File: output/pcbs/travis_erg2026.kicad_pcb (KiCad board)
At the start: 2 copper layers, 163.7 x 159.6 mm, 161 parts

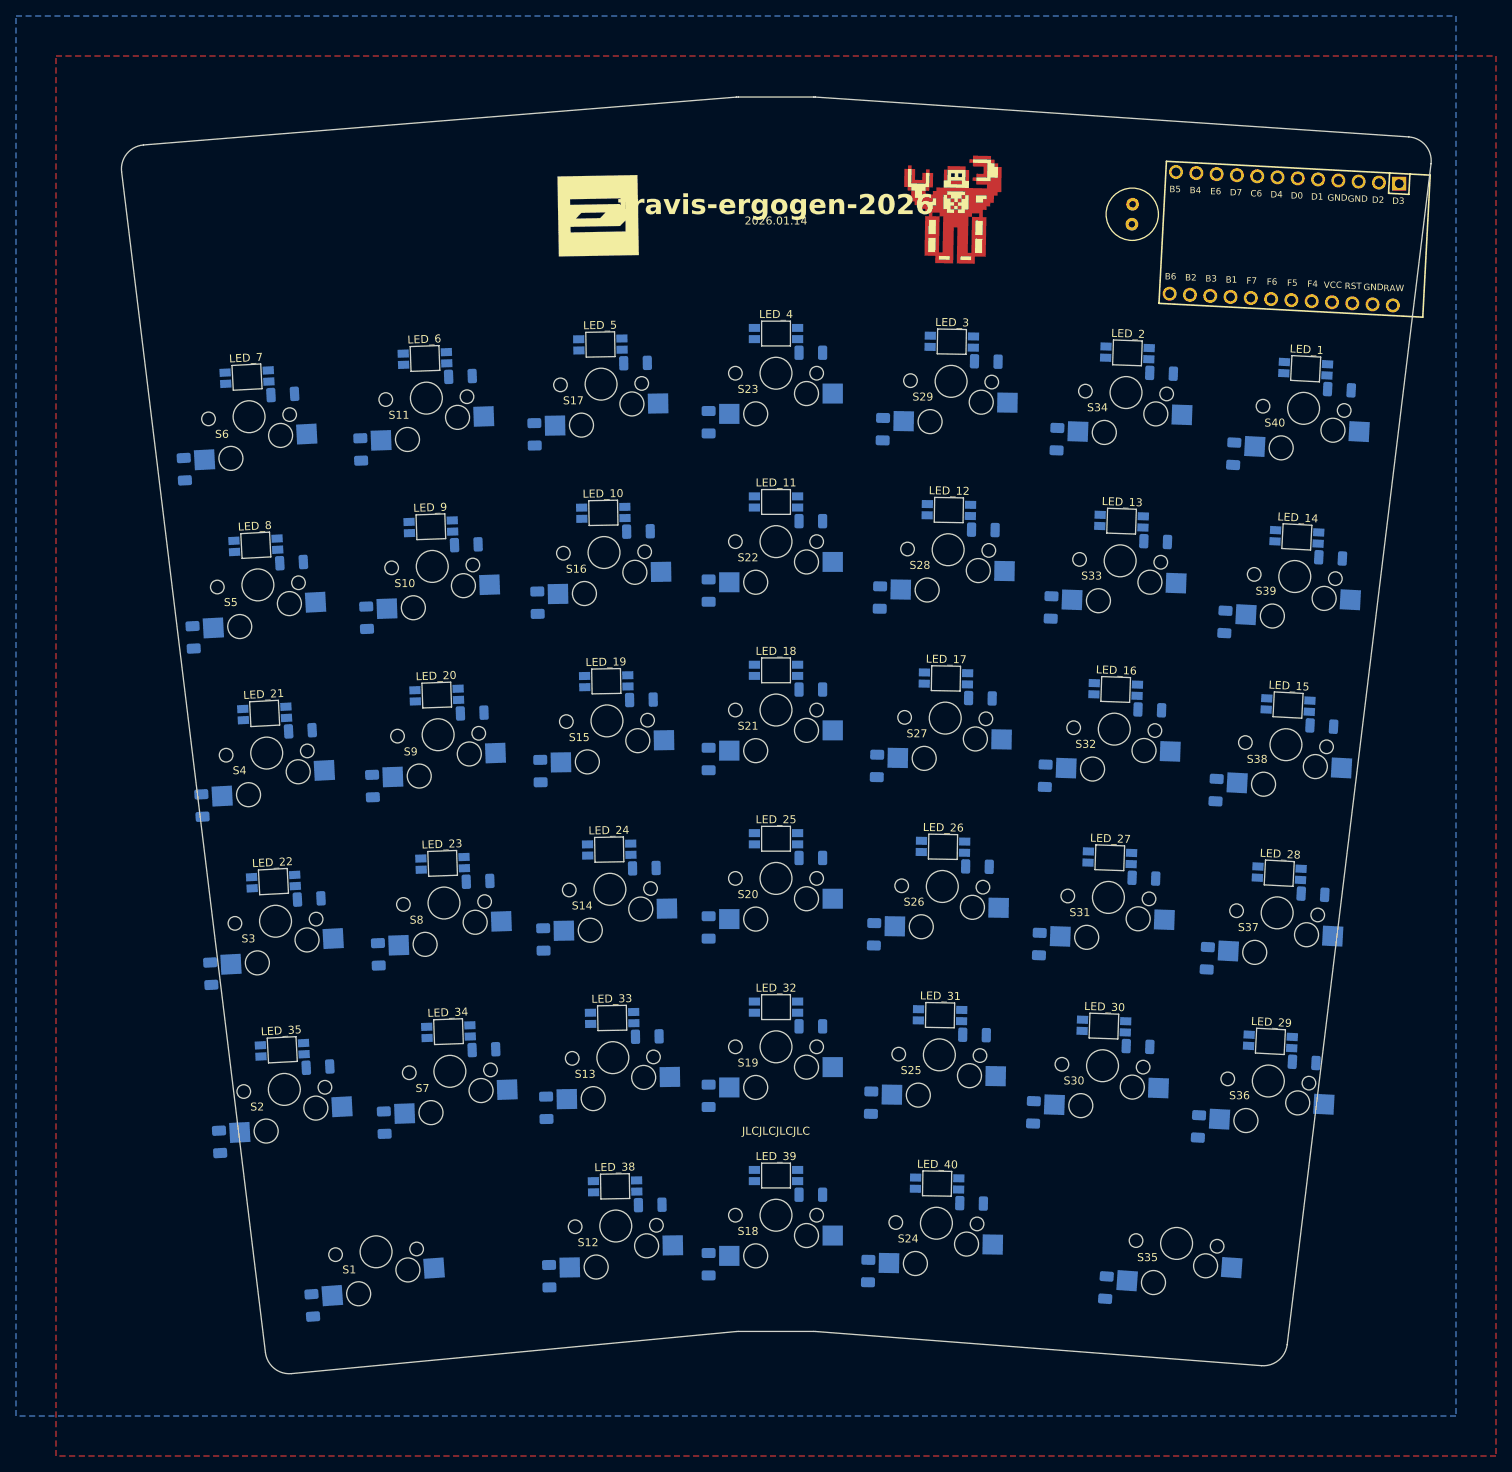
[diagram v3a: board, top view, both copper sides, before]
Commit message: led caps
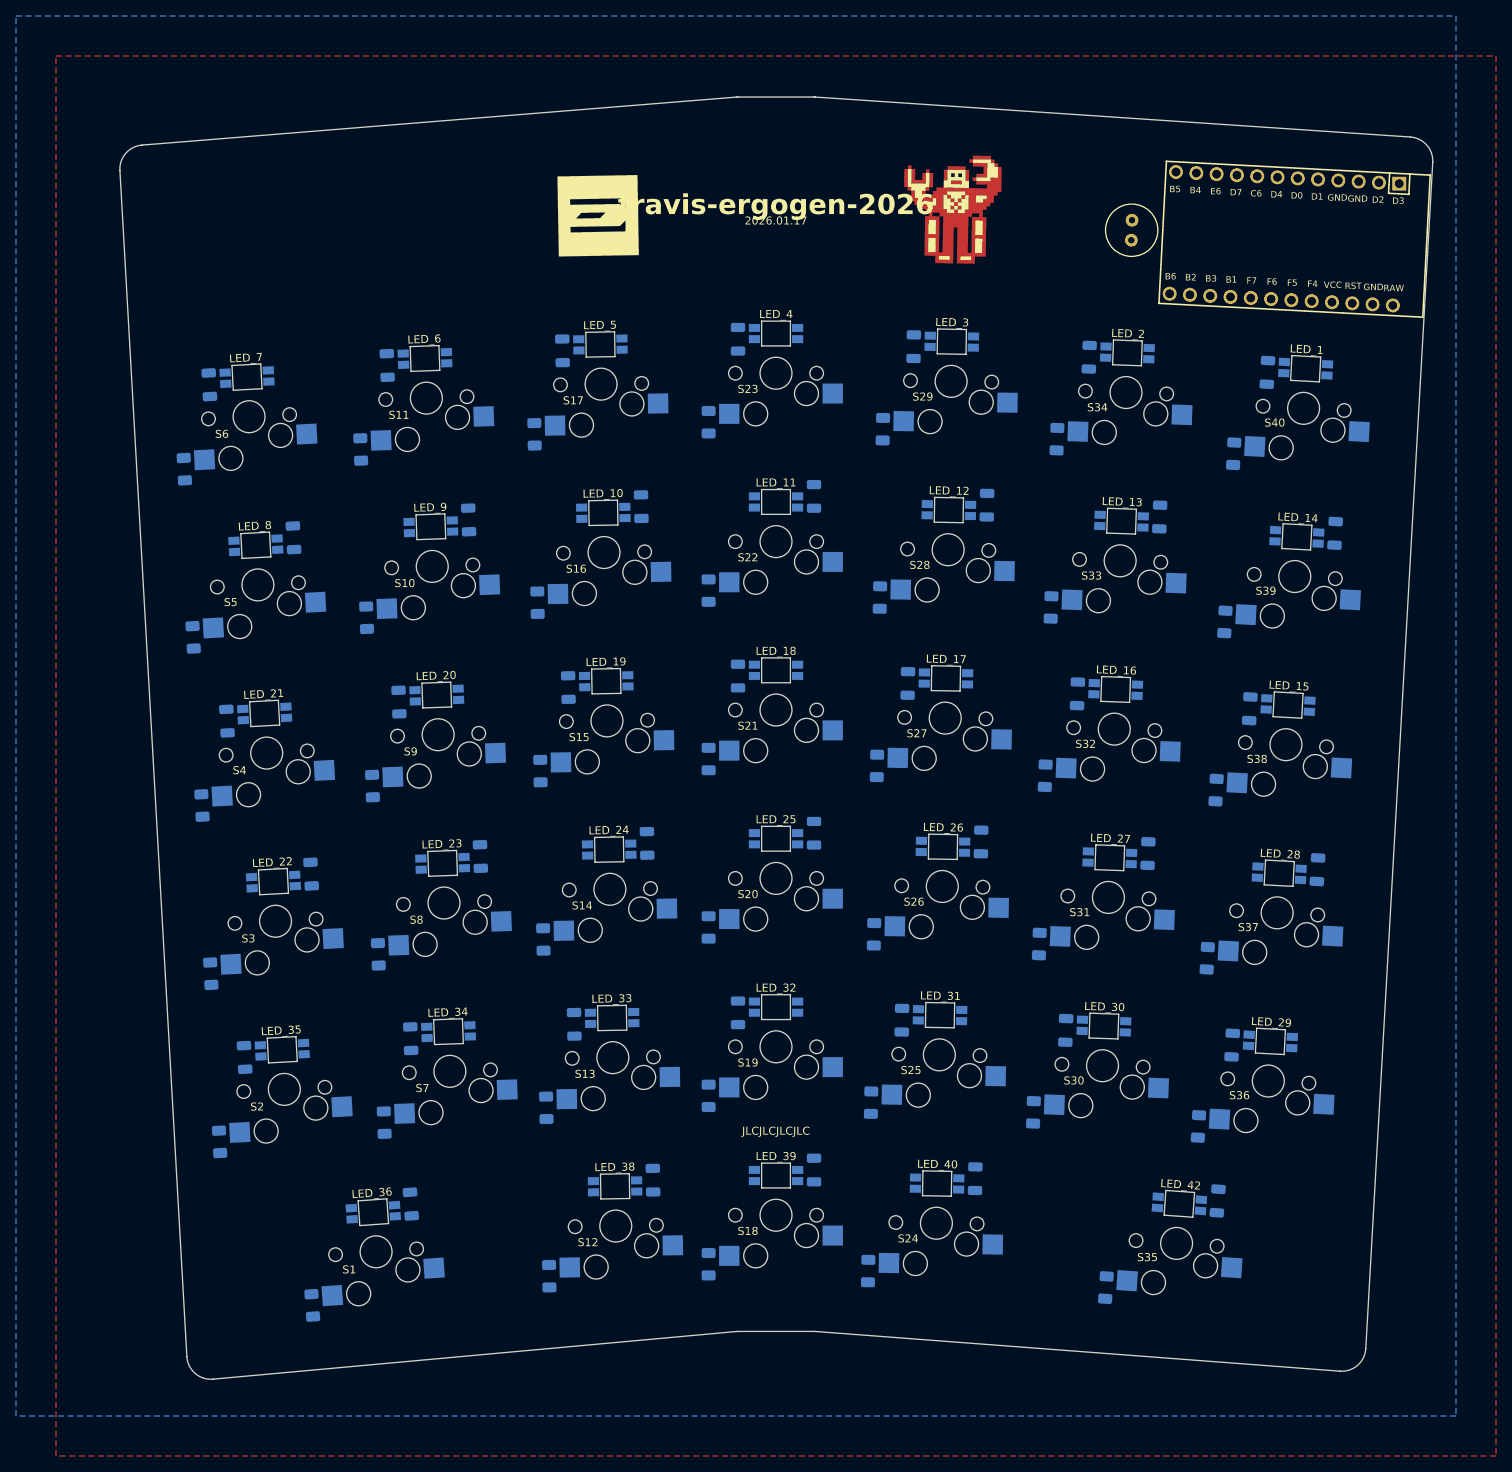
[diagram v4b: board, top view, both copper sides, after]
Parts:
- added C40: C_1206_3216Metric, C_1206_3216Metric, B.Cu at (177.7, 151.7)
- added C41: C_1206_3216Metric, C_1206_3216Metric, B.Cu at (179.9, 109.7)
- added LED39: SK6812mini-e, travis:led_SK6812mini-e (per-key, single-side), B.Cu at (172.9, 152.2)
- added LED40: SK6812mini-e, travis:led_SK6812mini-e (per-key, single-side), B.Cu at (175.1, 110.1)
- moved C33 90.5 mm to (114.8, 105.1), turned to 90 degrees
- moved C30 88.6 mm to (93.2, 106.3), turned to 91 degrees
- moved C27 88.6 mm to (71.6, 108.0), turned to 92 degrees
- moved LED32 87.5 mm to (110.0, 105.7), turned to 0 degrees
- moved LED29 85.6 mm to (88.4, 107.1), turned to 1 degrees
- moved LED26 85.6 mm to (66.9, 108.8), turned to 2 degrees
- moved LED38 84.7 mm to (160.4, 193.5), turned to -4 degrees
- moved C39 81.6 mm to (165.2, 193.1), turned to 86 degrees
- moved C38 50.9 mm to (158.0, 107.6), turned to 88 degrees
- moved C36 50.6 mm to (136.4, 106.1), turned to 89 degrees
- moved C25 48.8 mm to (49.7, 110.2), turned to 93 degrees
- moved LED37 48.2 mm to (153.2, 108.1), turned to -2 degrees
- moved LED35 47.9 mm to (131.6, 106.8), turned to -1 degrees
- moved LED24 46.1 mm to (45.0, 111.2), turned to 3 degrees
- moved LED22 43.2 mm to (59.7, 194.5), turned to 4 degrees
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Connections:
- LED22 pad 2: LED_23 -> LED_37
- LED22 pad 4: LED_22 -> LED_36
- LED23 pad 2: LED_9 -> LED_23
- LED23 pad 4: LED_8 -> LED_22
- LED24 pad 2: LED_24 -> LED_9
- LED24 pad 4: LED_23 -> LED_8
- LED25 pad 2: LED_10 -> LED_24
- LED25 pad 4: LED_9 -> LED_23
- LED26 pad 2: LED_39 -> LED_10
- LED26 pad 4: LED_38 -> LED_9
- LED27 pad 2: LED_25 -> LED_39
- LED27 pad 4: LED_24 -> LED_38
- LED28 pad 2: LED_11 -> LED_25
- LED28 pad 4: LED_10 -> LED_24
- LED29 pad 2: LED_40 -> LED_11
- LED29 pad 4: LED_39 -> LED_10
- LED30 pad 2: LED_26 -> LED_40
- LED30 pad 4: LED_25 -> LED_39
- LED31 pad 2: LED_12 -> LED_26
- LED31 pad 4: LED_11 -> LED_25
- LED32 pad 2: LED_41 -> LED_12
- LED32 pad 4: LED_40 -> LED_11
- LED33 pad 2: LED_27 -> LED_41
- LED33 pad 4: LED_26 -> LED_40
- LED34 pad 2: LED_13 -> LED_27
- LED34 pad 4: LED_12 -> LED_26
- LED35 pad 2: LED_28 -> LED_13
- LED35 pad 4: LED_27 -> LED_12
- LED36 pad 2: LED_14 -> LED_28
- LED36 pad 4: LED_13 -> LED_27
- LED37 pad 2: LED_29 -> LED_14
- LED37 pad 4: LED_28 -> LED_13
- LED38 pad 2: LED_13 -> (no net)
- LED38 pad 4: LED_14 -> LED_42
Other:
- board size 163.7 x 159.6 mm -> 164.1 x 160.3 mm
- board text added: "2026.01.17"
- board text added: "LED_36"
- board text added: "LED_42"
- board text removed: "2026.01.14"

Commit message: stabs, diodes, caps labels
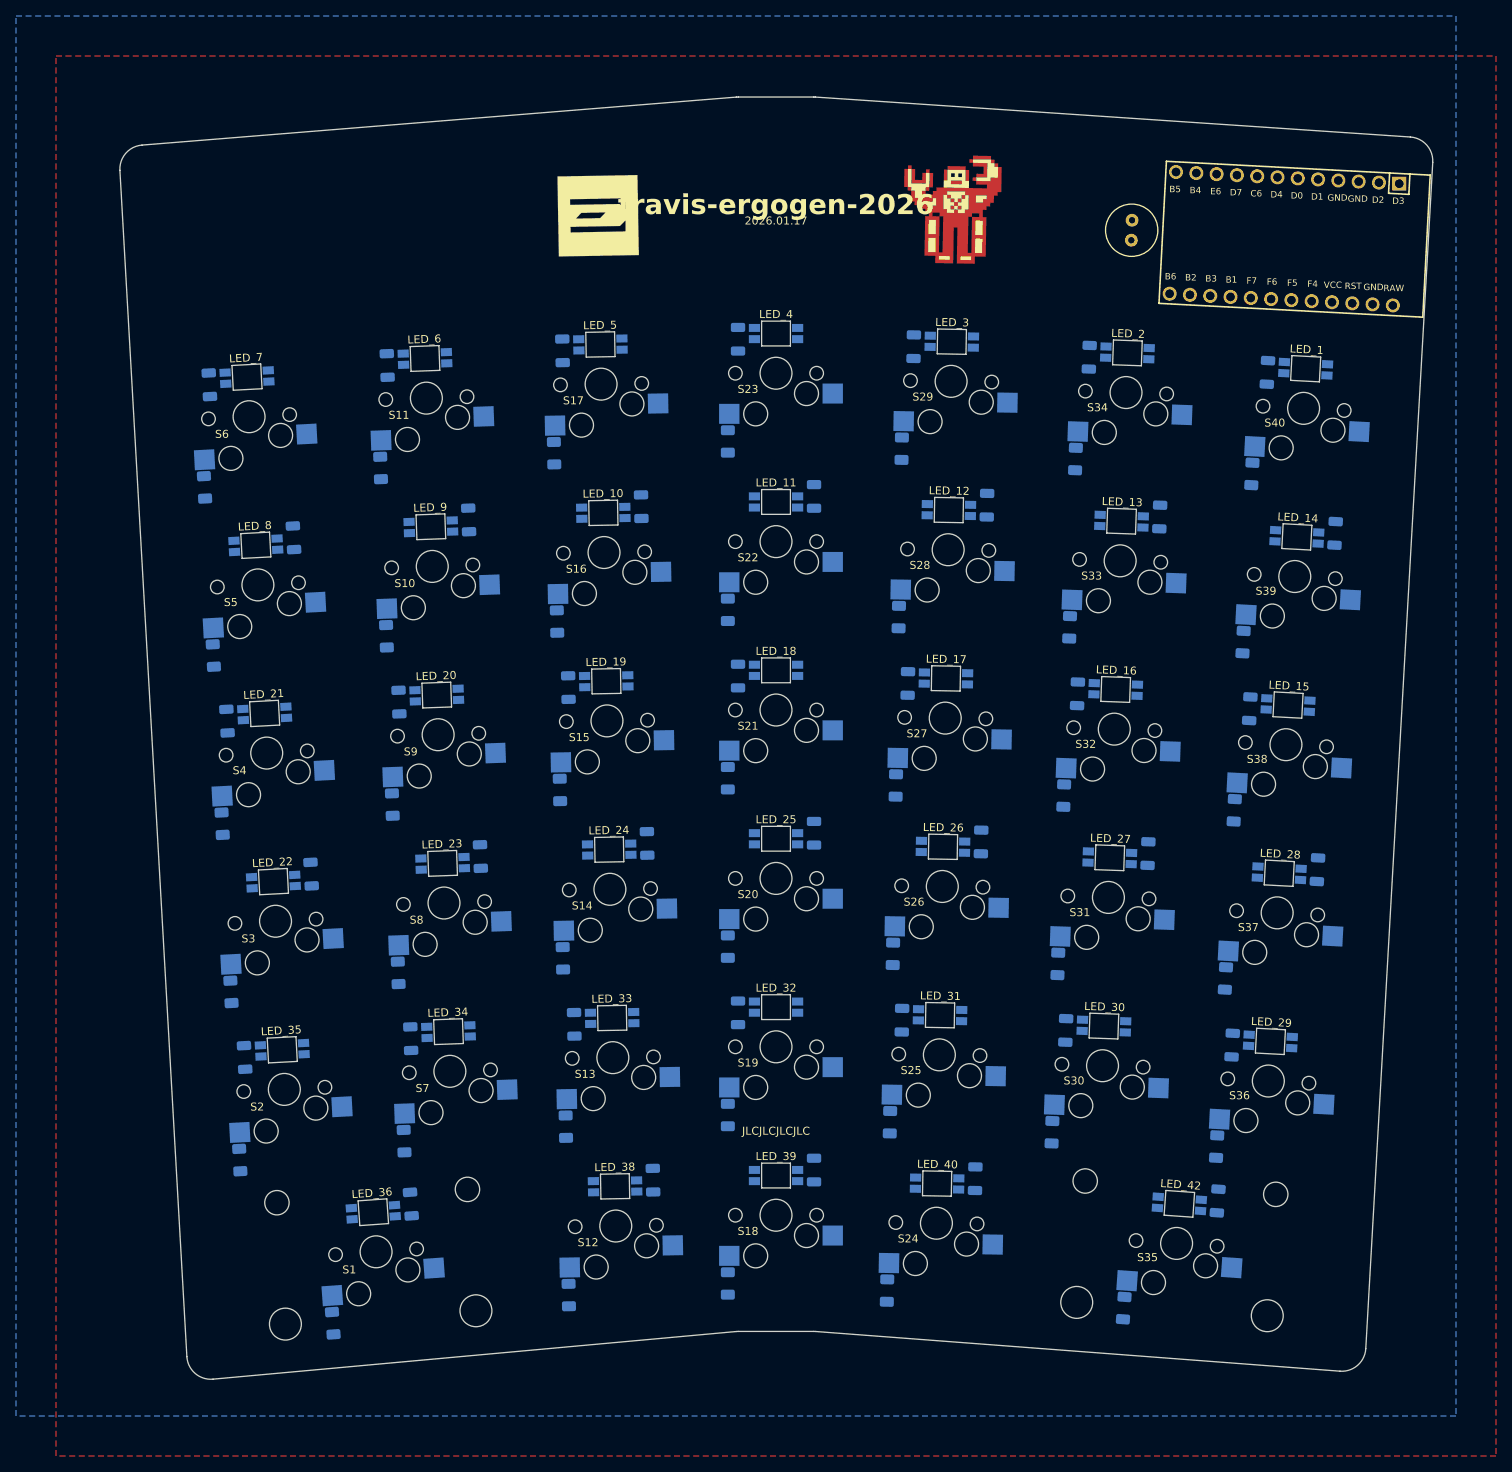
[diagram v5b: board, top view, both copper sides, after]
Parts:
- added STAB2u1: Stabilizer_MX_2.00u, ScottoKeebs_Stabilizer:Stabilizer_MX_2.00u, F.Cu at (60.0, 199.5)
- added STAB2u2: Stabilizer_MX_2.00u, ScottoKeebs_Stabilizer:Stabilizer_MX_2.00u, F.Cu at (160.1, 198.4)
- C1: value 10V 1000uF -> 10V 470uF
- moved D25 3.39 mm to (124.2, 183.3)
- moved D27 3.39 mm to (125.0, 141.2)
- moved D28 3.39 mm to (125.3, 120.1)
- moved D29 3.39 mm to (125.7, 99.1)
- moved D24 3.39 mm to (123.9, 204.3)
- moved D26 3.39 mm to (124.6, 162.2)
- moved D35 3.39 mm to (153.5, 206.5)
- moved D2 3.39 mm to (43.0, 188.0)
- moved D3 3.39 mm to (41.9, 167.0)
- moved D4 3.39 mm to (40.8, 146.0)
- moved D5 3.39 mm to (39.7, 124.9)
- moved D6 3.39 mm to (38.6, 103.9)
- moved D10 3.39 mm to (61.3, 122.5)
- moved D11 3.39 mm to (60.6, 101.5)
- moved D7 3.39 mm to (63.5, 185.6)
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
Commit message: holes, oled options
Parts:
- added HOLE1: , travis:MountingHole_2.2mm_M2_Pad_Via, F.Cu at (30.7, 64.0)
- added HOLE2: , travis:MountingHole_2.2mm_M2_Pad_Via, F.Cu at (189.4, 62.9)
- added HOLE3: , travis:MountingHole_2.2mm_M2_Pad_Via, F.Cu at (181.0, 211.7)
- added HOLE4: , travis:MountingHole_2.2mm_M2_Pad_Via, F.Cu at (39.1, 212.7)
- added OLED1: OLED, lib:OLED_headers, F.Cu at (32.1, 67.1)
- added OLED2: OLED, lib:OLED_headers, F.Cu at (59.9, 82.5)
- added OLED3: OLED, lib:OLED_headers, F.Cu at (71.1, 58.5)
- added OLED4: OLED, lib:OLED_headers, F.Cu at (104.0, 79.1)
- added OLED5: OLED, lib:OLED_headers, F.Cu at (116.0, 55.6)
- moved C1 1.00 mm to (154.4, 74.0)
- moved MCU1 1.00 mm to (173.5, 73.8)
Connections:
- LED27 pad 2: LED_39 -> LED_38
- LED27 pad 4: LED_38 -> LED_37
- LED30 pad 2: LED_40 -> LED_39
- LED30 pad 4: LED_39 -> LED_38
- LED33 pad 2: LED_41 -> LED_40
- LED33 pad 4: LED_40 -> LED_39
- LED38 pad 4: LED_42 -> LED_40
- MCU1 pad 10: row4 -> row3
- MCU1 pad 11: row5 -> row4
- MCU1 pad 12: B5 -> row5
- MCU1 pad 13: col0 -> LED_1
- MCU1 pad 14: col1 -> col0
- MCU1 pad 15: col2 -> col1
- MCU1 pad 16: col3 -> col2
- MCU1 pad 17: col4 -> col3
- MCU1 pad 18: col5 -> col4
- MCU1 pad 19: col6 -> col5
- MCU1 pad 20: LED_1 -> col6
- MCU1 pad 5: D1 -> sda
- MCU1 pad 6: row0 -> scl
- MCU1 pad 7: row1 -> row0
- MCU1 pad 8: row2 -> row1
- MCU1 pad 9: row3 -> row2
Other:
- outline, holes or cut-outs redrawn
- board text added: "2026.01.19"
- board text added: "LED_37"
- board text removed: "2026.01.17"
- board text removed: "LED_42"

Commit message: scotto keebs 2040 promicro
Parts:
- C1: value 10V 470uF -> 6.3V 1000uF
- MCU1: value Arduino Pro Micro -> RP2040 Pro Micro; footprint Arduino_Pro_Micro -> RP2040_Pro_Micro
- moved C1 10.5 mm to (143.9, 73.7)
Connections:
- MCU1 pad 1: D3 -> GP10
- MCU1 pad 10: row3 -> row2
- MCU1 pad 11: row4 -> row3
- MCU1 pad 12: row5 -> row4
- MCU1 pad 13: LED_1 -> row5
- MCU1 pad 14: col0 -> GP12
- MCU1 pad 15: col1 -> GP13
- MCU1 pad 16: col2 -> GP14
- MCU1 pad 17: col3 -> GP15
- MCU1 pad 18: col4 -> GP16
- MCU1 pad 19: col5 -> LED_1
- MCU1 pad 2: D2 -> D3
- MCU1 pad 20: col6 -> col0
- MCU1 pad 21: VCC -> col1
- MCU1 pad 22: RST -> col2
- MCU1 pad 23: GND -> col3
- MCU1 pad 24: RAW -> col4
- MCU1 pad 3: GND -> D2
- MCU1 pad 5: sda -> GND
- MCU1 pad 6: scl -> sda
- MCU1 pad 7: row0 -> scl
- MCU1 pad 8: row1 -> row0
- MCU1 pad 9: row2 -> row1
